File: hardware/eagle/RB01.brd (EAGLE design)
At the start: 50 x 31 mm, 10 parts, among them J1 CON_TERMINAL_BLOCK_03-5MM, J2 CON_TERMINAL_BLOCK_02-5MM, K1 JS-M1A-12V-5, Q1 BC547

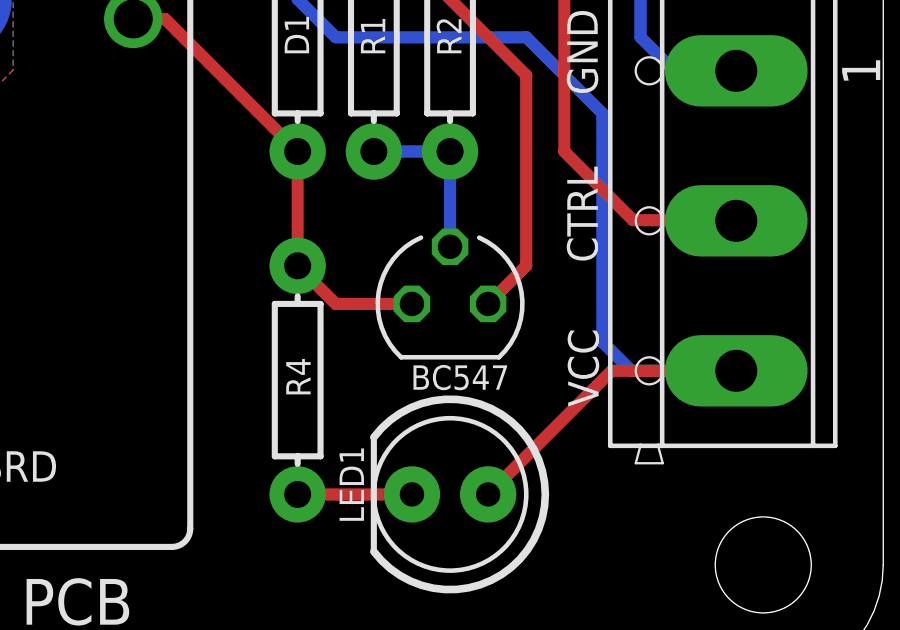
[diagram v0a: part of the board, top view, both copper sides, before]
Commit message: BC337s instead of BC546s
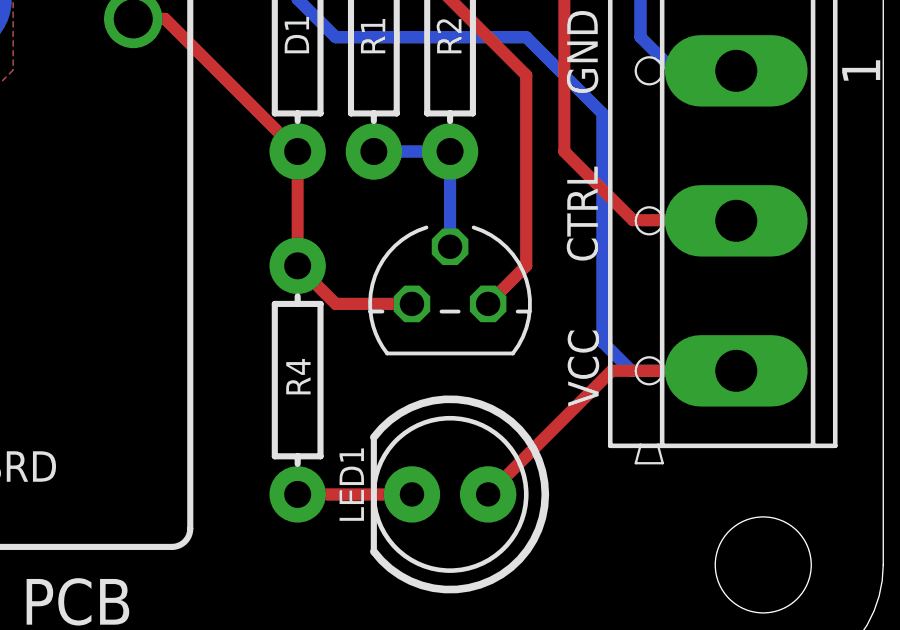
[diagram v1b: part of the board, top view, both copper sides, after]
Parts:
- Q1: value BC547 -> BC337; device transistor-small-signal:SOT54A -> transistor:TO92
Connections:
- net COIL: now also Q1.3; no longer Q1.C
- net GND: now also Q1.1; no longer Q1.E
- net N$6: now also Q1.2; no longer Q1.B
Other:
- board text removed: "BC547"
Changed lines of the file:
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@@
 <text x="2.143" y="8.858" size="1.016" layer="21" ratio="15">Normally</text>
 <text x="40.483" y="14.073" size="1.016" layer="21" ratio="15" rot="R90">CTRL</text>
-<text x="37.546" y="10.652" size="0.8128" layer="21" font="vector" ratio="15" rot="R180">BC547</text>
 <text x="15.192" y="6.772" size="1.016" layer="21" font="vector" ratio="15">Songle SRD</text>
 <rectangle x1="11.4681" y1="12.5349" x2="17.0307" y2="12.5603" layer="22"/>
@@
 <element name="J1" library="dp_devices" package="TERMINAL_BLOCK_3P_5" value="CON_TERMINAL_BLOCK_03-5MM" x="44.65" y="15.47" smashed="yes" rot="R90"/>
 <element name="J2" library="dp_devices" package="TERMINAL_BLOCK_2P_5" value="CON_TERMINAL_BLOCK_02-5MM" x="5.5" y="15.5" smashed="yes" rot="R270"/>
-<element name="Q1" library="transistor-small-signal" package="SOT54A" value="BC547" x="35.56" y="12.7" smashed="yes"/>
+<element name="Q1" library="transistor" package="TO92" value="BC337" x="35.56" y="12.7" smashed="yes">
+<attribute name="VALUE" x="33.909" y="10.033" size="0.8128" layer="27" font="vector" ratio="10"/>
+</element>
 <element name="K1" library="relay" package="JS-M1A" value="JS-M1A-12V-5" x="19" y="15.5" smashed="yes" rot="R90">
 <attribute name="OC_NEWARK" value="13P4555" x="19" y="15.5" size="1.778" layer="27" rot="R90" display="off"/>
@@
 <contactref element="J1" pad="1"/>
 <wire x1="41.91" y1="24.13" x2="38.1" y2="27.94" width="0.4064" layer="16"/>
-<contactref element="Q1" pad="E"/>
+<contactref element="Q1" pad="1"/>
 <wire x1="41.91" y1="24.13" x2="41.91" y2="21.59" width="0.4064" layer="16"/>
 <wire x1="41.91" y1="21.59" x2="43.18" y2="20.32" width="0.4064" layer="16"/>
@@
 <contactref element="R1" pad="P$1"/>
 <wire x1="35.56" y1="17.78" x2="33.02" y2="17.78" width="0.4064" layer="16"/>
-<contactref element="Q1" pad="B"/>
+<contactref element="Q1" pad="2"/>
 <wire x1="35.56" y1="14.605" x2="35.56" y2="17.78" width="0.4064" layer="16"/>
 </signal>
@@
 <contactref element="R4" pad="P$1"/>
 <wire x1="30.48" y1="13.97" x2="30.48" y2="17.78" width="0.4064" layer="1"/>
-<contactref element="Q1" pad="C"/>
+<contactref element="Q1" pad="3"/>
 <wire x1="34.29" y1="12.7" x2="31.75" y2="12.7" width="0.4064" layer="1"/>
 <wire x1="31.75" y1="12.7" x2="30.48" y2="13.97" width="0.4064" layer="1"/>
@@
 <wire x1="40.64" y1="19.05" x2="38.1" y2="21.59" width="0.4064" layer="16"/>
 <wire x1="36.83" y1="6.35" x2="40.95" y2="10.47" width="0.4064" layer="1"/>
-<wire x1="40.64" y1="10.16" x2="43.18" y2="10.16" width="0" layer="19" extent="1-16"/>
-<wire x1="43.18" y1="10.16" x2="44.45" y2="8.89" width="0" layer="19" extent="1-16"/>
-<wire x1="44.45" y1="8.89" x2="45.72" y2="8.89" width="0" layer="19" extent="1-16"/>
 <wire x1="45.1" y1="10.47" x2="40.95" y2="10.47" width="0.4064" layer="1"/>
-<wire x1="40.95" y1="10.47" x2="40.64" y2="10.16" width="0" layer="19" extent="1-16"/>
 </signal>
 </signals>

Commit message: Magic Smoke logo
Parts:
- added U$2: (no value), SparkFun:OSHW-LOGO-S
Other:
- board text added: "/Users/thomasprice/Documents/eagle/logo/Magic_Smoke_logo.bmp"

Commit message: tweak gerbers
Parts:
- moved U$2 1.30 mm to (19.1, 5.59)

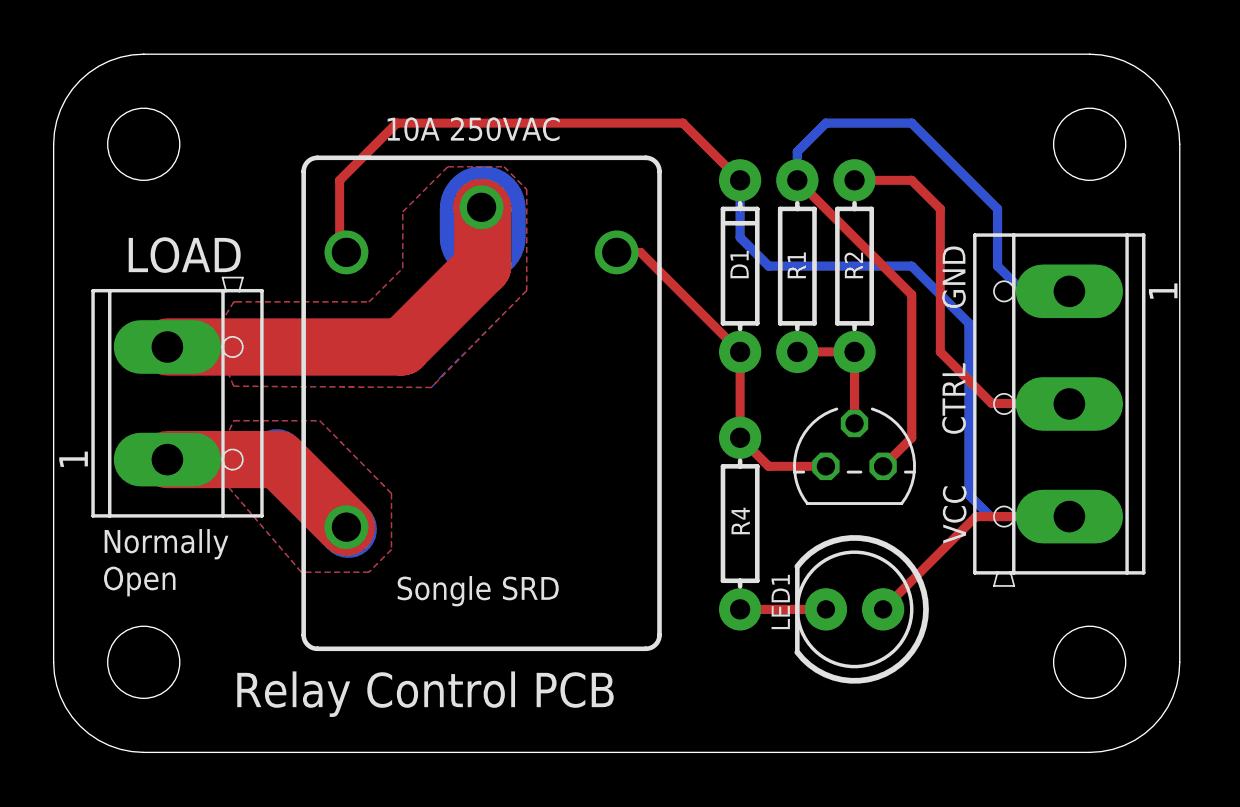
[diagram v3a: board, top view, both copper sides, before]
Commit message: JS-M1 relay package
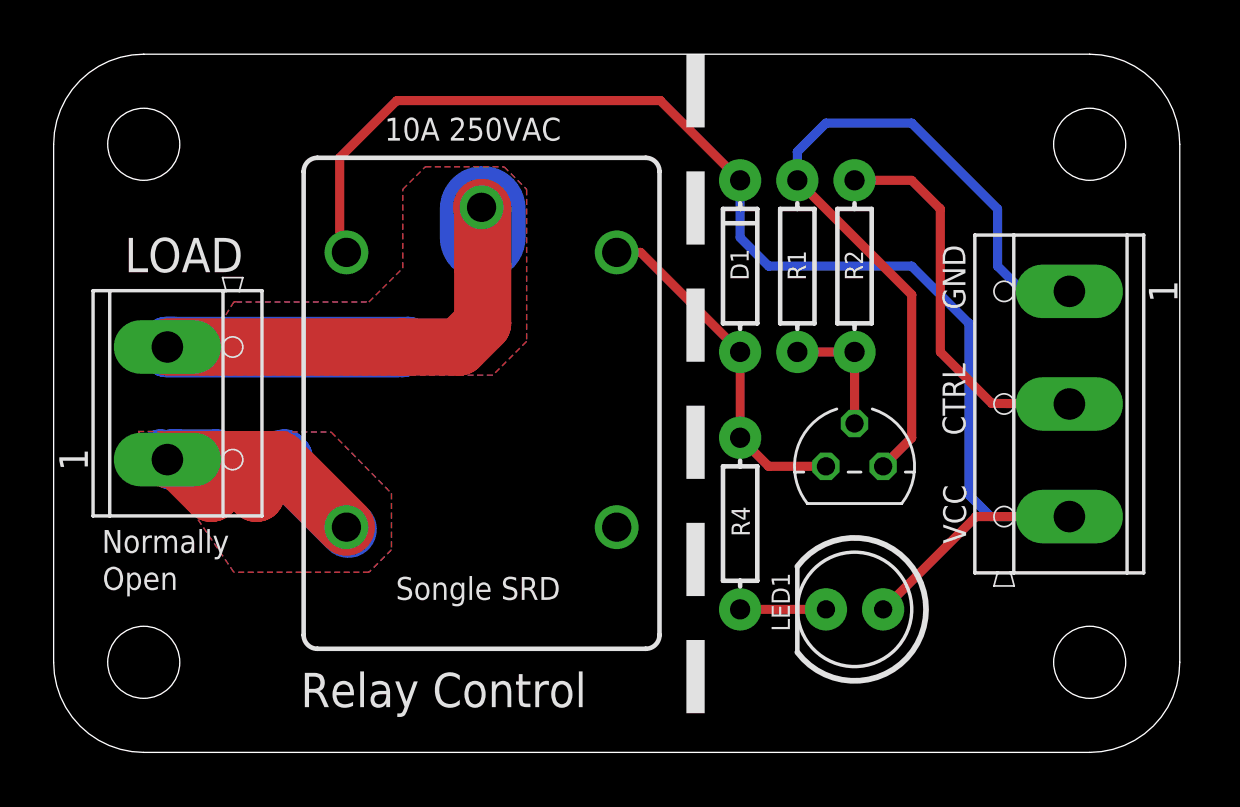
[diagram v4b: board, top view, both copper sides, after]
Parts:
- K1: value JS-M1A-12V-5 -> JS-M1-12V-5; device relay:JS-M1A -> relay:JS-M
- moved U$2 0.59 mm to (18.5, 5.58)
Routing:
- net LOAD2: track 29.8 -> 74.1 mm
- net LOAD1: track 18.5 -> 53.2 mm
- net VCC: track 59.9 -> 61.4 mm
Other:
- board text added: "DANGER"
- board text added: "HIGH"
- board text added: "Relay Control"
- board text added: "VOLTAGE"
- board text removed: "Relay Control PCB"
